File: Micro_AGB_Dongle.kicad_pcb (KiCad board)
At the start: 2 copper layers, 13.5 x 13.3 mm, 16 parts, among them J1 Conn_01x01_Male, J10 Conn_01x01_Male, J11 Conn_01x01_Male, J12 Conn_01x01_Male, J13 Conn_01x01_Male, J14 Conn_01x01_Male, J2 Conn_01x01_Male, J3 Conn_01x01_Male, J4 Conn_01x01_Male, J5 Conn_01x01_Male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

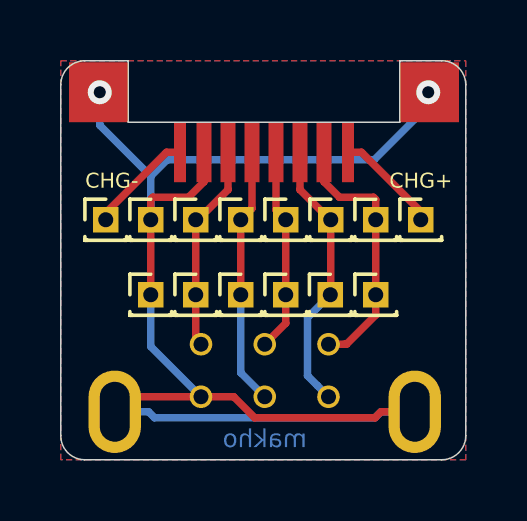
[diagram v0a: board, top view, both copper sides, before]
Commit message: Added M2 bolt holes & removed charging pins
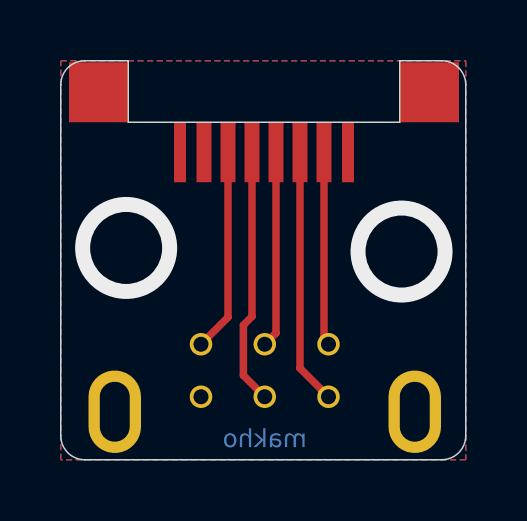
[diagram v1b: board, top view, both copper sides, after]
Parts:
- removed J1, J10, J11, J12, J13, J14, J2, J3, J4, J5, J6, J7, J8, J9: Conn_01x01_Male, Connector_PinHeader_1.00mm:PinHeader_1x01_P1.00mm_Vertical
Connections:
- EXP1 pad 7: Net-(EXP1-Pad7) -> unconnected-(EXP1-CHG+-Pad7)
- EXP1 pad 8: Net-(EXP1-Pad8) -> unconnected-(EXP1-CHG--Pad8)
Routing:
- net Net-(EXP1-GND): track 46.6 -> 0.00 mm, vias 2 -> 0
- net Net-(EXP1-Pad8): track 3.54 -> 0.00 mm
- net Net-(EXP1-Pad7): track 3.52 -> 0.00 mm
- net Net-(EXP1-PWR): track 8.78 -> 6.46 mm
- net Net-(EXP1-SO): track 9.20 -> 8.54 mm
- net (no net): vias 0 -> 2
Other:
- outline, holes or cut-outs redrawn
- net class Default removed
- board text removed: "CHG+"
- board text removed: "CHG-"
